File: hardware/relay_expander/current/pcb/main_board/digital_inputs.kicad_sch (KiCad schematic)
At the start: 22 parts, among them J12 Screw_Terminal_01x02, J13 Screw_Terminal_01x02, J14 Screw_Terminal_01x02, J15 Screw_Terminal_01x02, U4 TCMT4100, U5 TCMT4100

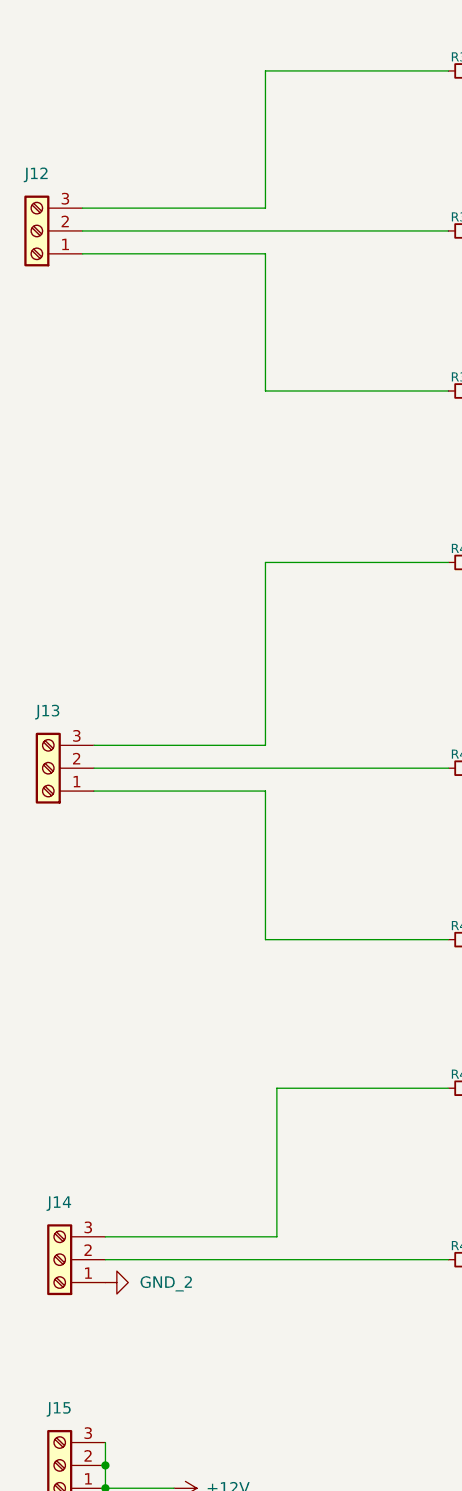
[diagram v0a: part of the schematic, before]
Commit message: [ADD] lauout for relay expander pcb
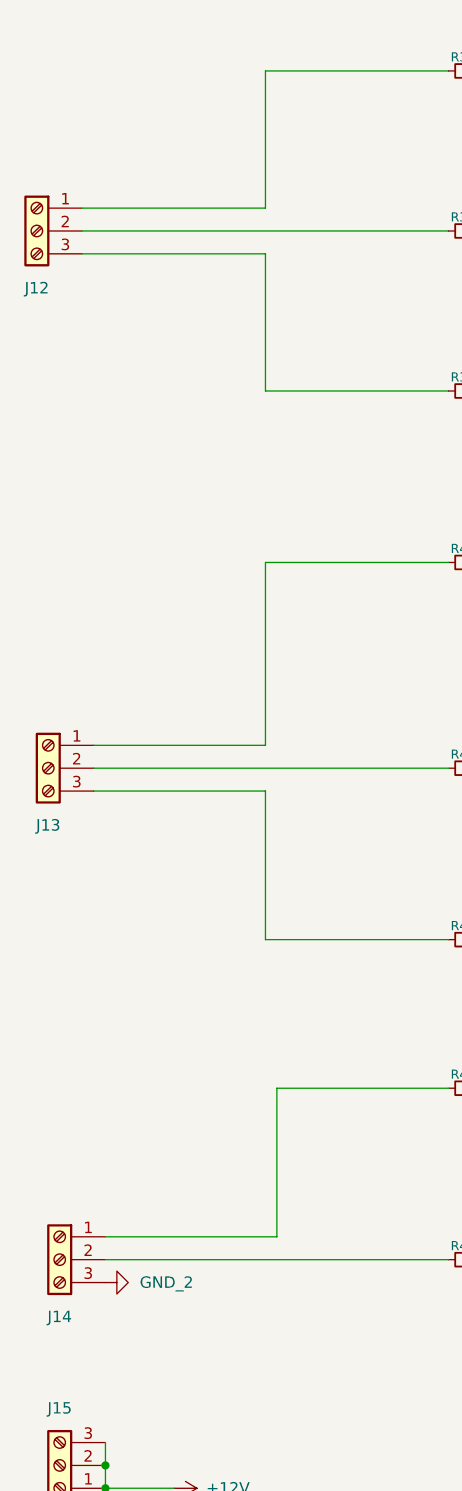
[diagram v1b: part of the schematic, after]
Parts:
- J12, J13, J14, J15: footprint Project_Parts_Footprints_Lib:TerminalBlock_Phoenix_MPT-0,5-3-2.54_1x03_P2.54mm_Horizontal -> footprints:Terminal_block_1x3_2,54
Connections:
- net GND_2: now also J14.3 (Pin_3); no longer J14.1 (Pin_1)
- net at R39.2: now also J12.3 (Pin_3); no longer J12.1 (Pin_1)
- net at R37.2: now also J12.1 (Pin_1); no longer J12.3 (Pin_3)
- net at R42.2: now also J13.3 (Pin_3); no longer J13.1 (Pin_1)
- net at R40.2: now also J13.1 (Pin_1); no longer J13.3 (Pin_3)
- net at R43.2: now also J14.1 (Pin_1); no longer J14.3 (Pin_3)
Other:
- moved on the sheet: J12, J13, J14
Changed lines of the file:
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@@
 			)
 		)
-		(property "Footprint" "Project_Parts_Footprints_Lib:TerminalBlock_Phoenix_MPT-0,5-3-2.54_1x03_P2.54mm_Horizontal"
+		(property "Footprint" "footprints:Terminal_block_1x3_2,54"
 			(at 90.17 180.34 0)
 			(hide yes)
@@
 	(symbol
 		(lib_id "Connector:Screw_Terminal_01x03")
-		(at 87.63 43.18 180)
+		(at 87.63 43.18 0)
+		(mirror y)
 		(unit 1)
 		(body_style 1)
@@
 		(in_pos_files yes)
 		(dnp no)
-		(fields_autoplaced yes)
 		(property "Reference" "J12"
-			(at 87.63 36.83 0)
+			(at 87.63 49.53 0)
 			(show_name no)
 			(do_not_autoplace no)
@@
 		)
 		(property "Value" "Screw_Terminal_01x02"
-			(at 85.09 40.6401 0)
-			(hide yes)
-			(show_name no)
-			(do_not_autoplace no)
-			(effects
-				(font
-					(size 1.27 1.27)
-				)
-				(justify left)
-			)
-		)
-		(property "Footprint" "Project_Parts_Footprints_Lib:TerminalBlock_Phoenix_MPT-0,5-3-2.54_1x03_P2.54mm_Horizontal"
+			(at 85.09 45.7199 0)
+			(hide yes)
+			(show_name no)
+			(do_not_autoplace no)
+			(effects
+				(font
+					(size 1.27 1.27)
+				)
+				(justify left)
+			)
+		)
+		(property "Footprint" "footprints:Terminal_block_1x3_2,54"
 			(at 87.63 43.18 0)
 			(hide yes)
@@
 	(symbol
 		(lib_id "Connector:Screw_Terminal_01x03")
-		(at 88.9 102.87 180)
+		(at 88.9 102.87 0)
+		(mirror y)
 		(unit 1)
 		(body_style 1)
@@
 		(in_pos_files yes)
 		(dnp no)
-		(fields_autoplaced yes)
 		(property "Reference" "J13"
-			(at 88.9 96.52 0)
+			(at 88.9 109.22 0)
 			(show_name no)
 			(do_not_autoplace no)
@@
 		)
 		(property "Value" "Screw_Terminal_01x02"
-			(at 86.36 100.3301 0)
-			(hide yes)
-			(show_name no)
-			(do_not_autoplace no)
-			(effects
-				(font
-					(size 1.27 1.27)
-				)
-				(justify left)
-			)
-		)
-		(property "Footprint" "Project_Parts_Footprints_Lib:TerminalBlock_Phoenix_MPT-0,5-3-2.54_1x03_P2.54mm_Horizontal"
+			(at 86.36 105.4099 0)
+			(hide yes)
+			(show_name no)
+			(do_not_autoplace no)
+			(effects
+				(font
+					(size 1.27 1.27)
+				)
+				(justify left)
+			)
+		)
+		(property "Footprint" "footprints:Terminal_block_1x3_2,54"
 			(at 88.9 102.87 0)
 			(hide yes)
@@
 	(symbol
 		(lib_id "Connector:Screw_Terminal_01x03")
-		(at 90.17 157.48 180)
+		(at 90.17 157.48 0)
+		(mirror y)
 		(unit 1)
 		(body_style 1)
@@
 		(in_pos_files yes)
 		(dnp no)
-		(fields_autoplaced yes)
 		(property "Reference" "J14"
-			(at 90.17 151.13 0)
+			(at 90.17 163.83 0)
 			(show_name no)
 			(do_not_autoplace no)
@@
 		)
 		(property "Value" "Screw_Terminal_01x02"
-			(at 87.63 154.9401 0)
-			(hide yes)
-			(show_name no)
-			(do_not_autoplace no)
-			(effects
-				(font
-					(size 1.27 1.27)
-				)
-				(justify left)
-			)
-		)
-		(property "Footprint" "Project_Parts_Footprints_Lib:TerminalBlock_Phoenix_MPT-0,5-3-2.54_1x03_P2.54mm_Horizontal"
+			(at 87.63 160.0199 0)
+			(hide yes)
+			(show_name no)
+			(do_not_autoplace no)
+			(effects
+				(font
+					(size 1.27 1.27)
+				)
+				(justify left)
+			)
+		)
+		(property "Footprint" "footprints:Terminal_block_1x3_2,54"
 			(at 90.17 157.48 0)
 			(hide yes)
